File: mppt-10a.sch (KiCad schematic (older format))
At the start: 6 parts

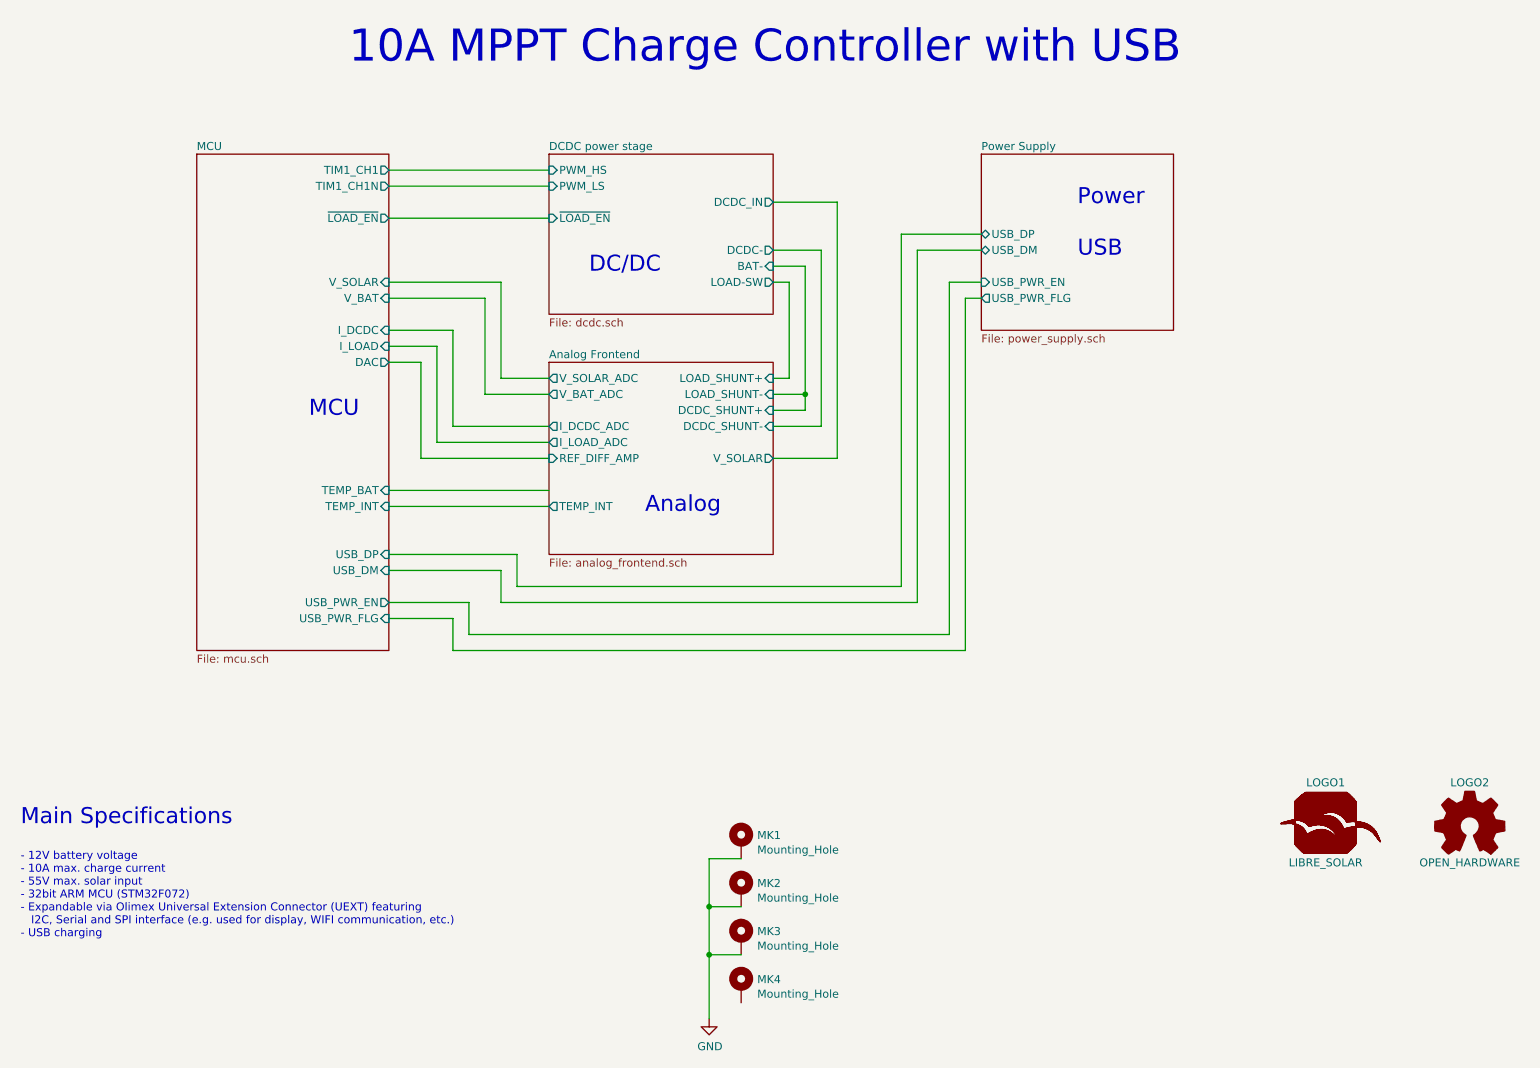
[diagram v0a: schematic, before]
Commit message: Several improvements (v0.4) after first tests
- Ultra-low-power MCU STM32L072
- Larger screw terminals
- USB power supply replaced by more efficient SMPS
- High-side load switch with P-MOS
- High-side current measurement to include USB current in load measurement
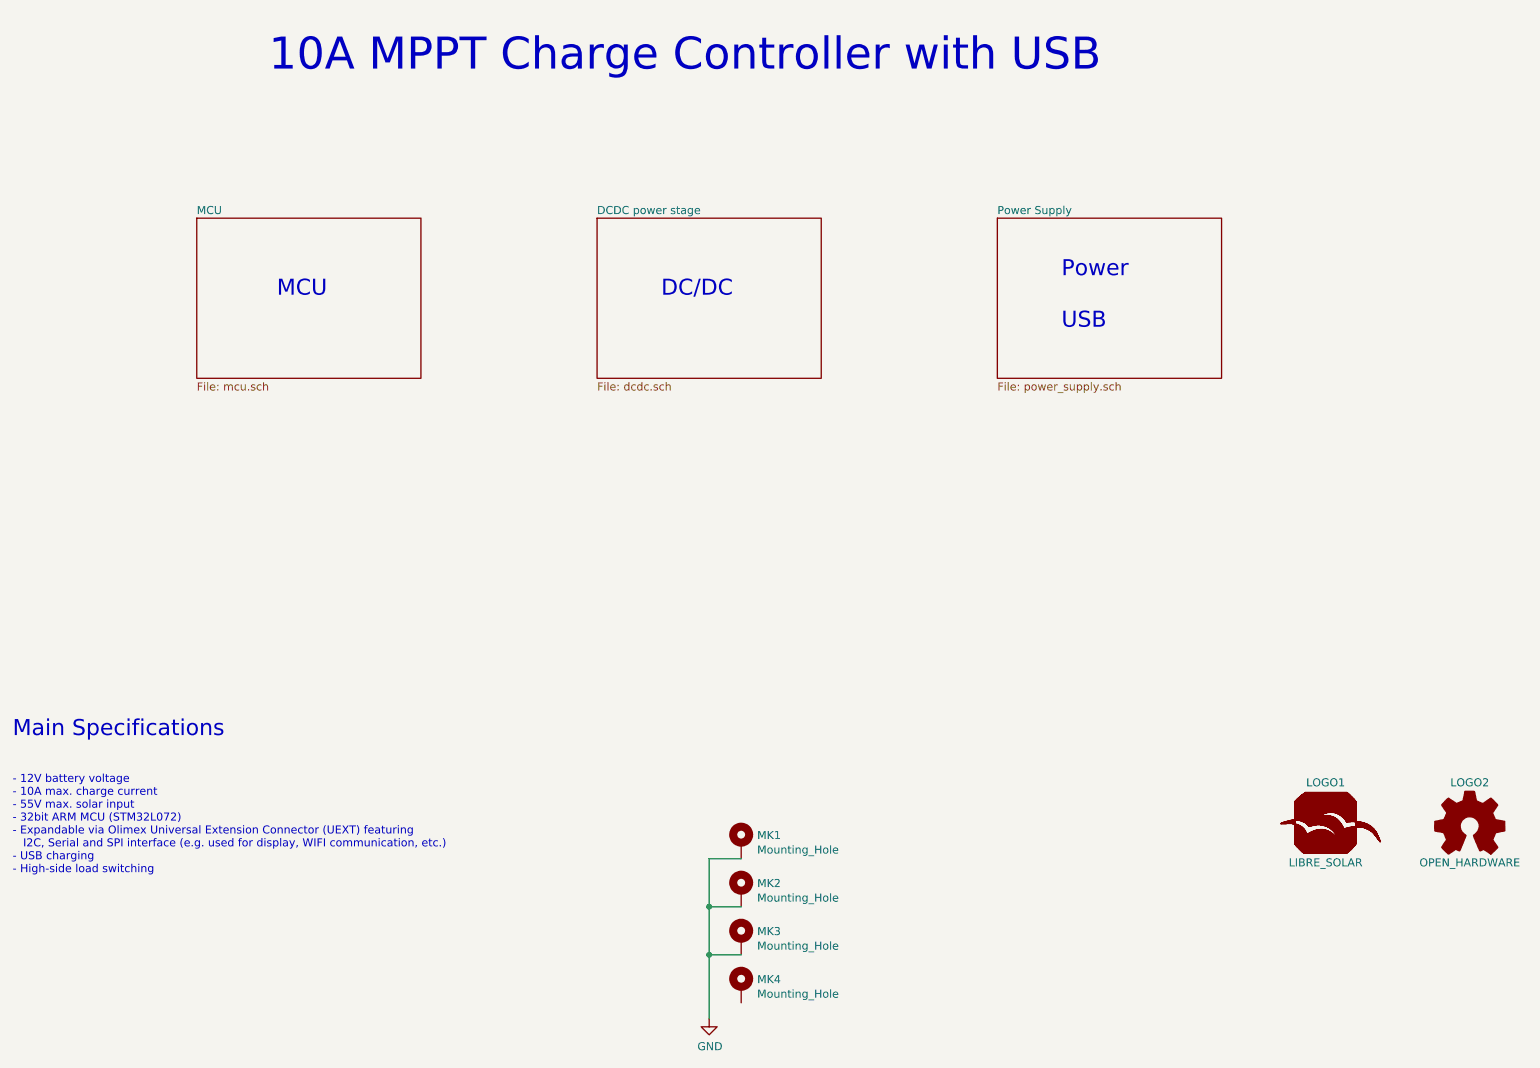
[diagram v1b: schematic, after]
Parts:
- LOGO1, LOGO2, MK1, MK2, MK3, MK4: Config (none) -> +info
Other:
- note added: "- 12V battery voltage\n- 10A max. charge current\n- 55V max. solar input\n- 32bit ARM MCU (STM32L072)\n- Expandable via Olimex Universal Extension Connector (UEXT) featuring\n I2C, Serial and SPI interface (e.g. used for display, WIFI communication, etc.)\n- USB charging\n- High-side load switching\n"
- note removed: "- 12V battery voltage\n- 10A max. charge current\n- 55V max. solar input\n- 32bit ARM MCU (STM32F072)\n- Expandable via Olimex Universal Extension Connector (UEXT) featuring\n I2C, Serial and SPI interface (e.g. used for display, WIFI communication, etc.)\n- USB charging\n"
- note removed: "Analog"
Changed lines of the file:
@@
 EESchema Schematic File Version 4
+LIBS:mppt-10a-cache
 EELAYER 26 0
 EELAYER END
 $Descr A4 11693 8268
 encoding utf-8
-Sheet 1 5
+Sheet 1 4
 Title "10A MPPT Charge Controller with USB"
-Date "2018-05-14"
-Rev "0.2"
+Date "2018-08-23"
+Rev "0.4"
 Comp "Libre Solar"
 Comment1 "Author: Martin Jäger"
@@
 $EndDescr
 $Sheet
-S 4800 1900 1400 1000
+S 5100 2300 1400 1000
 U 58A68DC9
 F0 "DCDC power stage" 50
 F1 "dcdc.sch" 50
-F2 "PWM_HS" I L 4800 2000 50
-F3 "PWM_LS" I L 4800 2100 50
-F4 "BAT-" I R 6200 2600 50
-F5 "DCDC_IN" O R 6200 2200 50
-F6 "DCDC-" O R 6200 2500 50
-F7 "~LOAD_EN" I L 4800 2300 50
-F8 "LOAD-SW" O R 6200 2700 50
 $EndSheet
 $Sheet
-S 2600 1900 1200 3100
+S 2600 2300 1400 1000
 U 58A68DCB
 F0 "MCU" 50
 F1 "mcu.sch" 50
-F2 "TIM1_CH1N" O R 3800 2100 50
-F3 "TIM1_CH1" O R 3800 2000 50
-F4 "V_BAT" I R 3800 2800 50
-F5 "V_SOLAR" I R 3800 2700 50
-F6 "I_LOAD" I R 3800 3100 50
-F7 "I_DCDC" I R 3800 3000 50
-F8 "USB_DM" I R 3800 4500 50
-F9 "USB_DP" I R 3800 4400 50
-F10 "TEMP_INT" I R 3800 4100 50
-F11 "TEMP_BAT" I R 3800 4000 50
-F12 "DAC" O R 3800 3200 50
-F13 "~LOAD_EN" O R 3800 2300 50
-F14 "USB_PWR_EN" O R 3800 4700 50
-F15 "USB_PWR_FLG" I R 3800 4800 50
 $EndSheet
 $Sheet
-S 7500 1900 1200 1100
+S 7600 2300 1400 1000
 U 58C18D5C
 F0 "Power Supply" 50
 F1 "power_supply.sch" 50
-F2 "USB_DP" B L 7500 2400 50
-F3 "USB_DM" B L 7500 2500 50
-F4 "USB_PWR_EN" I L 7500 2700 50
-F5 "USB_PWR_FLG" O L 7500 2800 50
 $EndSheet
-Wire Wire Line
-	3800 2000 4800 2000
-Wire Wire Line
-	4800 2100 3800 2100
-Text Notes 3550 1350 0    200  ~ 0
+Text Notes 3050 1400 0    200  ~ 0
 10A MPPT Charge Controller with USB
-Text Notes 1500 6100 0    100  ~ 0
+Text Notes 1450 5550 0    100  ~ 0
 Main Specifications
-Text Notes 1500 6800 0    50   ~ 0
-- 12V battery voltage\n- 10A max. charge current\n- 55V max. solar input\n- 32bit ARM MCU (STM32F072)\n- Expandable via Olimex Universal Extension Connector (UEXT) featuring\n   I2C, Serial and SPI interface (e.g. used for display, WIFI communication, etc.)\n- USB charging\n
+Text Notes 1450 6400 0    50   ~ 0
+- 12V battery voltage\n- 10A max. charge current\n- 55V max. solar input\n- 32bit ARM MCU (STM32L072)\n- Expandable via Olimex Universal Extension Connector (UEXT) featuring\n   I2C, Serial and SPI interface (e.g. used for display, WIFI communication, etc.)\n- USB charging\n- High-side load switching\n
 $Comp
 L Project:Logo_Open_Hardware_Small LOGO2
@@
 F 2 "Symbol:OSHW-Logo_5.7x6mm_SilkScreen" H 10550 6100 60  0001 C CNN
 F 3 "" H 10550 6100 60  0001 C CNN
+F 4 "+info" H 0   0   50  0001 C CNN "Config"
 	1    10550 6100
 	1    0    0    -1
@@
 F 2 "LibreSolar:LIBRESOLAR_LOGO" H 9670 6090 60  0001 C CNN
 F 3 "" H 9670 6090 60  0001 C CNN
+F 4 "+info" H 9650 6100 50  0001 C CNN "Config"
 	1    9650 6100
 	1    0    0    -1
 $EndComp
-Wire Wire Line
-	6200 2200 6600 2200
-$Sheet
-S 4800 3200 1400 1200
-U 58E22D17
-F0 "Analog Frontend" 50
-F1 "analog_frontend.sch" 50
-F2 "V_SOLAR" O R 6200 3800 50
-F3 "TEMP_INT" O L 4800 4100 50
-F4 "DCDC_SHUNT+" I R 6200 3500 50
-F5 "LOAD_SHUNT+" I R 6200 3300 50
-F6 "LOAD_SHUNT-" I R 6200 3400 50
-F7 "DCDC_SHUNT-" I R 6200 3600 50
-F8 "V_SOLAR_ADC" O L 4800 3300 50
-F9 "V_BAT_ADC" O L 4800 3400 50
-F10 "I_LOAD_ADC" O L 4800 3700 50
-F11 "I_DCDC_ADC" O L 4800 3600 50
-F12 "REF_DIFF_AMP" I L 4800 3800 50
-$EndSheet
-Wire Wire Line
-	3800 2300 4800 2300
-Text Notes 5050 2650 0    100  ~ 0
+Text Notes 5500 2800 0    100  ~ 0
 DC/DC
-Text Notes 3300 3550 0    100  ~ 0
+Text Notes 3100 2800 0    100  ~ 0
 MCU
-Text Notes 5400 4150 0    100  ~ 0
-Analog
-Text Notes 8100 2550 0    100  ~ 0
+Text Notes 8000 3000 0    100  ~ 0
 Power\n\nUSB
-Wire Wire Line
-	3800 2700 4500 2700
-Wire Wire Line
-	4500 2700 4500 3300
-Wire Wire Line
-	4500 3300 4800 3300
-Wire Wire Line
-	4800 3400 4400 3400
-Wire Wire Line
-	4400 3400 4400 2800
-Wire Wire Line
-	4400 2800 3800 2800
-Wire Wire Line
-	3800 3000 4200 3000
-Wire Wire Line
-	4200 3000 4200 3600
-Wire Wire Line
-	4200 3600 4800 3600
-Wire Wire Line
-	4800 3700 4100 3700
-Wire Wire Line
-	4100 3700 4100 3100
-Wire Wire Line
-	4100 3100 3800 3100
-Wire Wire Line
-	3800 3200 4000 3200
-Wire Wire Line
-	4000 3200 4000 3800
-Wire Wire Line
-	4000 3800 4800 3800
-Wire Wire Line
-	3800 4100 4800 4100
-Wire Wire Line
-	6200 2600 6400 2600
-Wire Wire Line
-	6200 2700 6300 2700
-Wire Wire Line
-	6200 2500 6500 2500
-Wire Wire Line
-	6300 2700 6300 3300
-Wire Wire Line
-	6300 3300 6200 3300
-Wire Wire Line
-	6200 3400 6400 3400
-Wire Wire Line
-	6400 2600 6400 3400
-Wire Wire Line
-	6400 3500 6200 3500
-Connection ~ 6400 3400
-Wire Wire Line
-	6200 3600 6500 3600
-Wire Wire Line
-	6500 3600 6500 2500
-Wire Wire Line
-	6600 2200 6600 3800
-Wire Wire Line
-	6600 3800 6200 3800
 $Comp
 L Mechanical:MountingHole_Pad MK1
@@
 F 2 "MountingHole:MountingHole_3.2mm_M3_Pad" H 6000 6200 50  0001 C CNN
 F 3 "" H 6000 6200 50  0001 C CNN
+F 4 "+info" H 0   0   50  0001 C CNN "Config"
 	1    6000 6200
 	1    0    0    -1
@@
 F 2 "MountingHole:MountingHole_3.2mm_M3_Pad" H 6000 6500 50  0001 C CNN
 F 3 "" H 6000 6500 50  0001 C CNN
+F 4 "+info" H 0   0   50  0001 C CNN "Config"
 	1    6000 6500
 	1    0    0    -1
@@
 F 2 "MountingHole:MountingHole_3.2mm_M3_Pad" H 6000 6800 50  0001 C CNN
 F 3 "" H 6000 6800 50  0001 C CNN
+F 4 "+info" H 0   0   50  0001 C CNN "Config"
 	1    6000 6800
 	1    0    0    -1
 $EndComp
-Wire Wire Line
-	6400 3400 6400 3500
-Wire Wire Line
-	3800 4000 4800 4000
 Wire Wire Line
 	6000 6300 5800 6300
@@
 $EndComp
 Connection ~ 5800 6900
-Wire Wire Line
-	3800 4400 4600 4400
-Wire Wire Line
-	4600 4400 4600 4600
-Wire Wire Line
-	4600 4600 7000 4600
-Wire Wire Line
-	7000 4600 7000 2400
-Wire Wire Line
-	7000 2400 7500 2400
-Wire Wire Line
-	3800 4500 4500 4500
-Wire Wire Line
-	4500 4500 4500 4700
-Wire Wire Line
-	4500 4700 7100 4700
-Wire Wire Line
-	7100 4700 7100 2500
-Wire Wire Line
-	7100 2500 7500 2500
 $Comp
 L Mechanical:MountingHole_Pad MK4
@@
 F 2 "MountingHole:MountingHole_3.2mm_M3_Pad" H 6000 7100 50  0001 C CNN
 F 3 "" H 6000 7100 50  0001 C CNN
+F 4 "+info" H 0   0   50  0001 C CNN "Config"
 	1    6000 7100
 	1    0    0    -1
@@
 Wire Wire Line
 	5800 6900 5800 7300
-Wire Wire Line
-	3800 4700 4300 4700
-Wire Wire Line
-	4300 4700 4300 4900
-Wire Wire Line
-	4300 4900 7300 4900
-Wire Wire Line
-	7300 4900 7300 2700
-Wire Wire Line
-	7300 2700 7500 2700
-Wire Wire Line
-	7500 2800 7400 2800
-Wire Wire Line
-	7400 2800 7400 5000
-Wire Wire Line
-	7400 5000 4200 5000
-Wire Wire Line
-	4200 5000 4200 4800
-Wire Wire Line
-	4200 4800 3800 4800
 $EndSCHEMATC

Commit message: Board shape adjusted and 6P6C connector added
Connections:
- net GND: now also MK4.1
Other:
- note added: "10A MPPT Solar Charge Controller with USB"
- note removed: "10A MPPT Charge Controller with USB"
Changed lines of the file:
@@
 EESchema Schematic File Version 4
-LIBS:mppt-10a-cache
-EELAYER 26 0
+LIBS:mptt-10a-cache
+EELAYER 29 0
 EELAYER END
 $Descr A4 11693 8268
@@
 Sheet 1 4
 Title "10A MPPT Charge Controller with USB"
-Date "2018-08-23"
-Rev "0.4"
-Comp "Libre Solar"
+Date "2019-03-24"
+Rev "0.5"
+Comp "Libre Solar / Connected Energy"
 Comment1 "Author: Martin Jäger"
-Comment2 "Website: http://libre.solar"
+Comment2 "Website: https://libre.solar"
 Comment3 ""
 Comment4 ""
@@
 F1 "power_supply.sch" 50
 $EndSheet
-Text Notes 3050 1400 0    200  ~ 0
-10A MPPT Charge Controller with USB
-Text Notes 1450 5550 0    100  ~ 0
+Text Notes 2300 1500 0    200  ~ 0
+10A MPPT Solar Charge Controller with USB
+Text Notes 2600 4700 0    100  ~ 0
 Main Specifications
-Text Notes 1450 6400 0    50   ~ 0
+Text Notes 2600 5500 0    50   ~ 0
 - 12V battery voltage\n- 10A max. charge current\n- 55V max. solar input\n- 32bit ARM MCU (STM32L072)\n- Expandable via Olimex Universal Extension Connector (UEXT) featuring\n   I2C, Serial and SPI interface (e.g. used for display, WIFI communication, etc.)\n- USB charging\n- High-side load switching\n
 $Comp
@@
 $EndComp
 Wire Wire Line
-	5800 6900 5800 7300
+	5800 6900 5800 7200
+Wire Wire Line
+	6000 7200 5800 7200
+Connection ~ 5800 7200
+Wire Wire Line
+	5800 7200 5800 7300
 $EndSCHEMATC
